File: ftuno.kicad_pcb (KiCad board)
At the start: 2 copper layers, 68.6 x 53.3 mm, 66 parts, among them CN1 AFC10-S04QCA-00, J1 Conn_01x08_Pin, J10 Conn_02x04_Odd_Even, J11 Conn_01x04_Socket, J2 Conn_01x08_Socket, J3 Conn_01x06_Pin, J4 Conn_01x06_Socket, J5 Conn_01x10_Pin, J6 Conn_01x10_Socket, J7 Conn_01x08_Pin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

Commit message: added UART level convertor, moved components, solved UART LED issue
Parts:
- added Q3: BSS138PS_C5224289, uno:SOT-363_L2.1-W1.3-P0.65-LS2.3-BL, F.Cu at (129.3, 67.0)
- added R15: 1k, Resistor_SMD:R_0402_1005Metric, F.Cu at (130.6, 76.2)
- added R16: 2k, Resistor_SMD:R_0402_1005Metric, F.Cu at (130.6, 78.2)
- added RN3: 2.2k, Resistor_SMD:R_Array_Convex_4x0603, F.Cu at (129.3, 70.9)
- RN1: value 1k -> 2.2k
- moved R13 10.3 mm to (132.8, 68.1), turned to 0 degrees
- moved X1 6.92 mm to (123.4, 67.8)
- moved J11 6.77 mm to (139.2, 70.7)
- moved U1 6.66 mm to (116.8, 71.1)
- moved C14 6.54 mm to (124.5, 71.1)
- moved C13 6.39 mm to (123.2, 71.1)
- moved J10 3.74 mm to (135.4, 70.7)
- moved R14 0.43 mm to (130.8, 80.8), turned to 0 degrees
- moved RN2 0.29 mm to (133.2, 57.4)
- moved Q2 0.15 mm to (133.1, 53.6)
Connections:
- C2 pad 1: VBUS -> +5V
- J10 pad 5: RESET -> SWRST
- J11 pad 1: +5V -> +3.3V
- R13 pad 1: SWRX -> Net-(Q3-S2)
- R13 pad 2: D2 -> SWRX
- R14 pad 1: SWTX -> Net-(Q3-S1)
- R14 pad 2: D3 -> SWTX
- U2 pad 16: VBUS -> +5V
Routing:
- net RX0: track 137.0 -> 95.2 mm, vias 5 -> 2
- net TX1: track 128.4 -> 90.7 mm
- net +5V: track 169.7 -> 198.8 mm, vias 10 -> 13
- net Net-(Q3-S1): track 0.00 -> 22.5 mm, vias 0 -> 3
- net A5/SCL: track 105.6 -> 124.1 mm, vias 6 -> 5
- net GND: track 83.5 -> 67.8 mm, vias 55 -> 42
- net D2: track 46.8 -> 60.8 mm, vias 2 -> 7
- net Net-(Q3-S2): track 0.00 -> 13.2 mm, vias 0 -> 2
- net VBUS: track 29.7 -> 16.8 mm
- net +3.3V: track 155.6 -> 144.4 mm, vias 16 -> 7
- net SCL: track 21.9 -> 14.0 mm
- net A2: track 15.5 -> 22.8 mm, vias 1 -> 0
- net D10: track 35.7 -> 29.2 mm
- net D9: track 34.9 -> 28.4 mm
- net D8: track 34.2 -> 27.7 mm
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
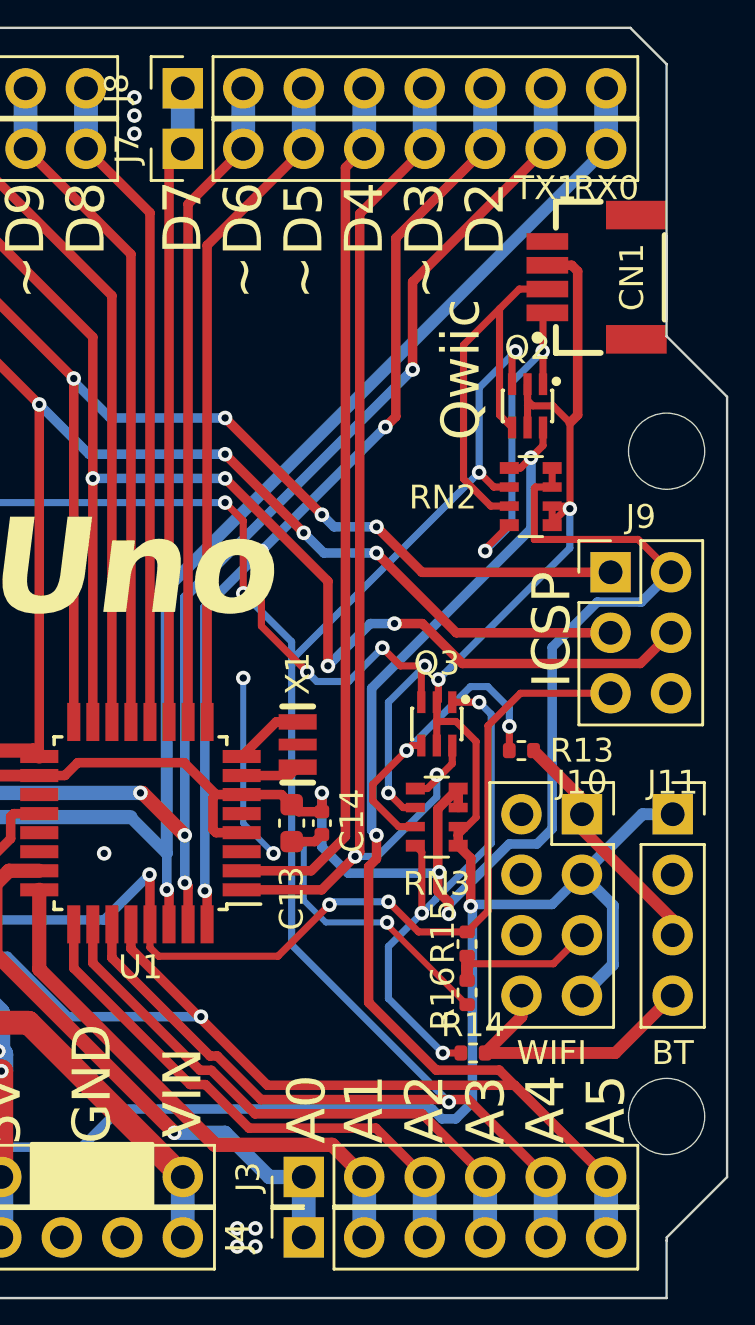
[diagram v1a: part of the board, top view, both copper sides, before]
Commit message: change softwareserial pin to D7, D8
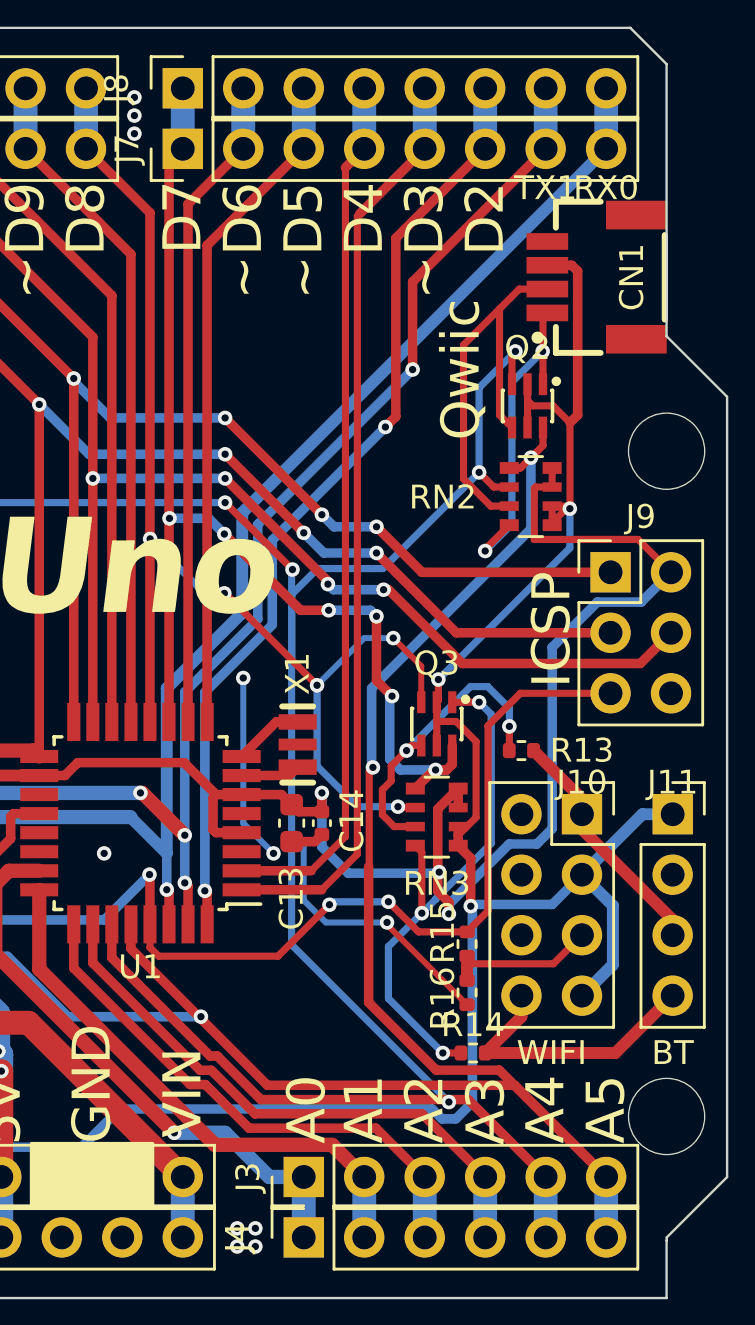
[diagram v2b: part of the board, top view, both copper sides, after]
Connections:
- Q3 pad 3: D2 -> D8
- Q3 pad 6: D3 -> D7
- RN3 pad 5: D3 -> D7
- RN3 pad 6: D2 -> D8
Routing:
- net D8: track 27.7 -> 52.7 mm, vias 0 -> 5
- net D7: track 26.9 -> 48.9 mm, vias 0 -> 6
- net D2: track 60.8 -> 40.0 mm, vias 7 -> 2
- net D3: track 47.2 -> 39.0 mm, vias 2 -> 0
- net D11/MOSI: track 61.5 -> 58.0 mm
- net A4/SDA: track 110.0 -> 111.6 mm
